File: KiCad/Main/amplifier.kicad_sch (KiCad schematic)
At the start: 37 parts, among them J3 Screw_Terminal_01x03, J4 Screw_Terminal_01x03, U3 TL074

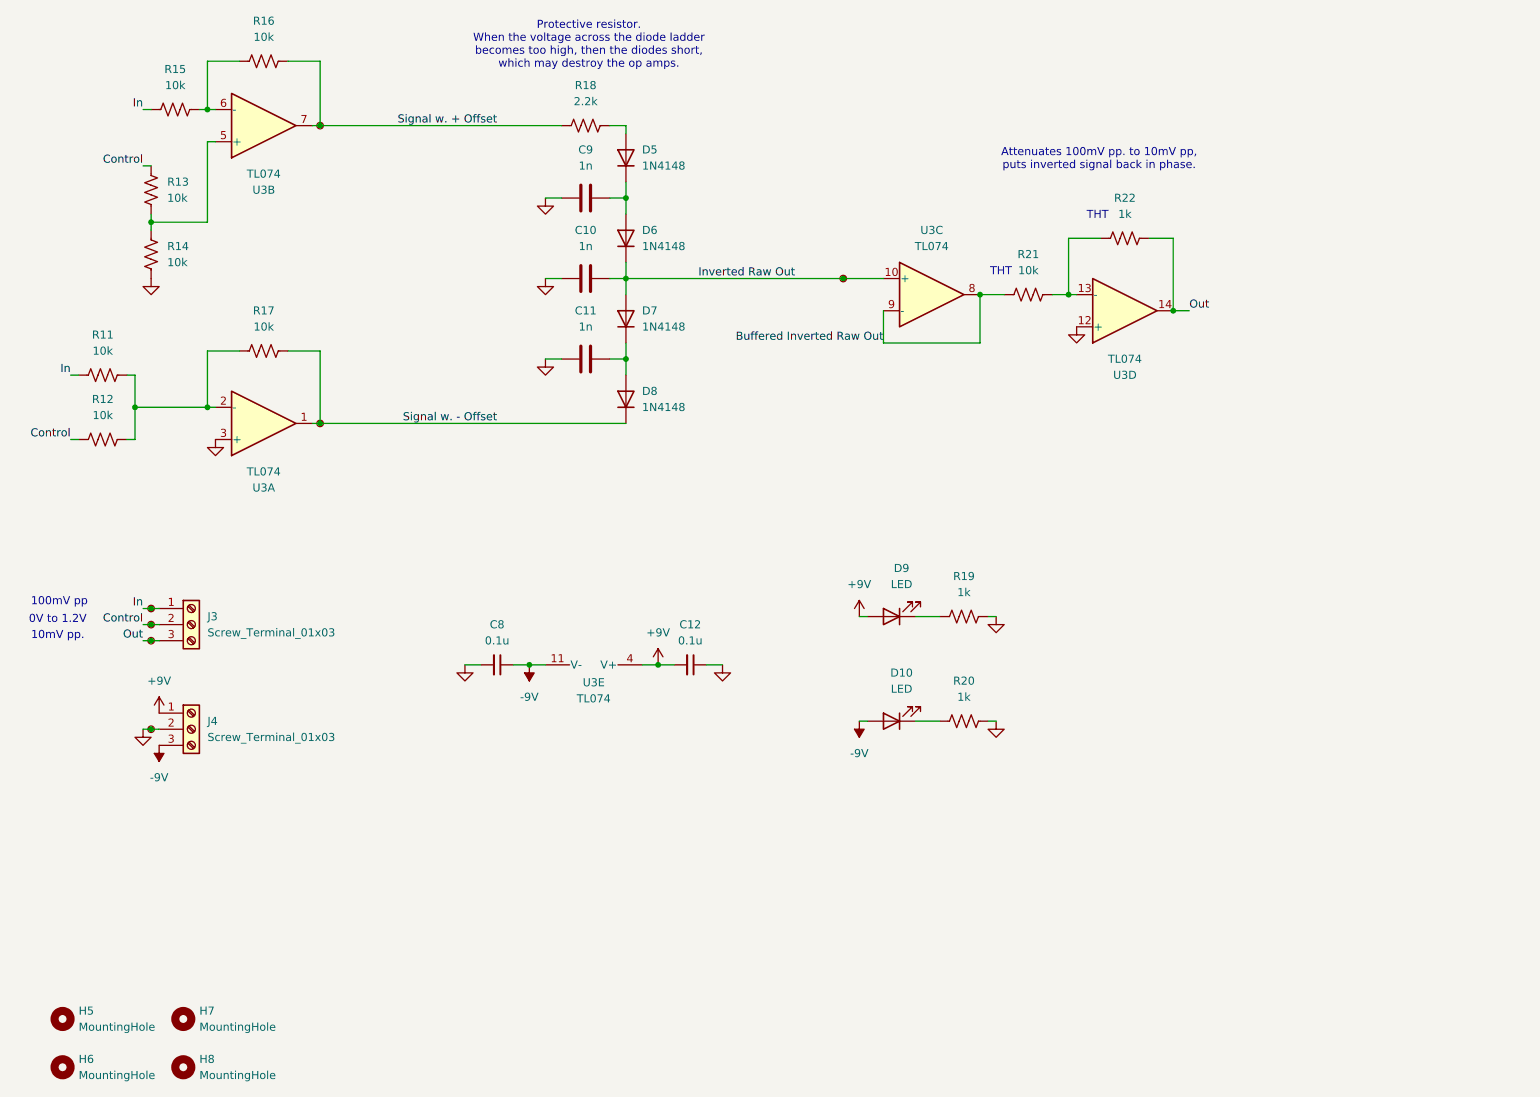
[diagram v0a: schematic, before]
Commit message: merged project into one combined board (excluding the buttons)
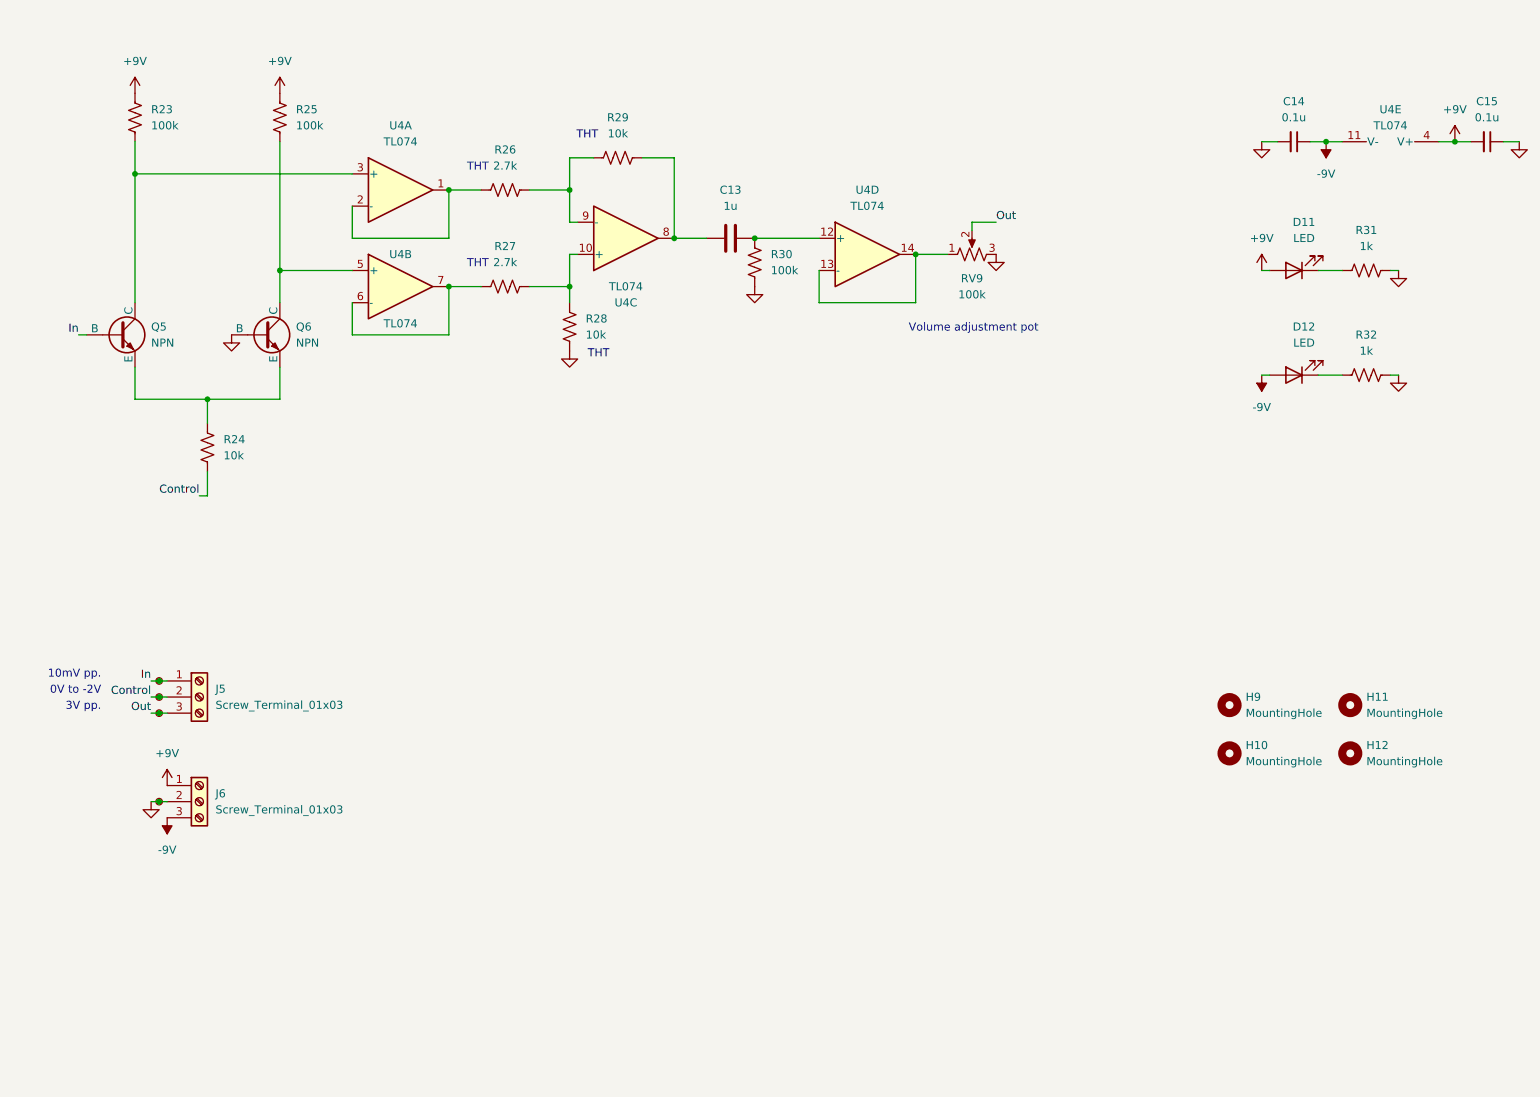
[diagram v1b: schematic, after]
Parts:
- removed C10, C11, C9: 1n, Capacitor_THT:C_Rect_L18.0mm_W5.0mm_P15.00mm_FKS3_FKP3, symbol Device:C
- removed D5, D6, D7, D8: 1N4148, Diode_THT:D_DO-35_SOD27_P7.62mm_Horizontal, symbol Diode:1N4148
- removed J3, J4: Screw_Terminal_01x03, Header 691137710003:691137710003, symbol Connector:Screw_Terminal_01x03
- removed R11, R12, R13, R14, R15, R16, R17: 10k, Resistor_SMD:R_0805_2012Metric, symbol Device:R_US
- removed R18: 2.2k, Resistor_SMD:R_0805_2012Metric, symbol Device:R_US
- removed R21: 10k, Resistor_THT:R_Axial_DIN0207_L6.3mm_D2.5mm_P7.62mm_Horizontal, symbol Device:R_US
- removed R22: 1k, Resistor_THT:R_Axial_DIN0207_L6.3mm_D2.5mm_P7.62mm_Horizontal, symbol Device:R_US
- removed TP10, TP11, TP12, TP6, TP7, TP8: TestPoint_Small, TestPoint:TestPoint_Keystone_5000-5004_Miniature, symbol Connector:TestPoint_Small
- removed U3: TL074, Package_DIP:DIP-14_W7.62mm, symbol Amplifier_Operational:TL074
- added C13: 1u, Capacitor_THT:C_Rect_L7.2mm_W4.5mm_P5.00mm, symbol Device:C
- added J5, J6: Screw_Terminal_01x03, Header 691137710003:691137710003, symbol Connector:Screw_Terminal_01x03
- added Q5, Q6: NPN, Package_TO_SOT_THT:TO-92, symbol Simulation_SPICE:NPN
- added R23, R25, R30: 100k, Resistor_SMD:R_0805_2012Metric, symbol Device:R_US
- added R24: 10k, Resistor_SMD:R_0805_2012Metric, symbol Device:R_US
- added R26, R27: 2.7k, Resistor_THT:R_Axial_DIN0207_L6.3mm_D2.5mm_P7.62mm_Horizontal, symbol Device:R_US
- added R28, R29: 10k, Resistor_THT:R_Axial_DIN0207_L6.3mm_D2.5mm_P7.62mm_Horizontal, symbol Device:R_US
- added RV9: 100k, Potentiometer_THT:Potentiometer_Bourns_PTV09A-2_Single_Horizontal, symbol Device:R_Potentiometer_US
- added TP14, TP15, TP16: TestPoint_Small, TestPoint:TestPoint_Keystone_5000-5004_Miniature, symbol Connector:TestPoint_Small
- added U4: TL074, Package_DIP:DIP-14_W7.62mm, symbol Amplifier_Operational:TL074
- renumbered C8 to C14, C12 to C15, D9 to D11, D10 to D12, H6 to H10, H7 to H11, H8 to H12, H5 to H9, R19 to R31, R20 to R32, TP9 to TP13
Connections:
- net +9V: now also J6.1 (Pin_1), R23.1, R25.1, U4.4 (V+)
- net -9V: now also J6.3 (Pin_3), U4.11 (V-)
- net Control: now also J5.2 (Pin_2), R24.2, TP14.1
- net GND: now also J6.2 (Pin_2), Q6.2 (B), R28.2, R30.2, RV9.3, TP16.1; no longer TP13.1
- net In: now also TP13.1, J5.1 (Pin_1), Q5.2 (B)
- net Out: now also J5.3 (Pin_3), RV9.2, TP15.1
- new net: C13.2, R30.1, U4.12 (+)
- new net: RV9.1, U4.13 (-), U4.14
- new net: R27.2, R28.1, U4.10 (+)
- new net: Q5.3 (E), Q6.3 (E), R24.1
- new net: R26.1, U4.1, U4.2 (-)
- new net: Q5.1 (C), R23.2, U4.3 (+)
- new net: C13.1, R29.2, U4.8
- new net: R26.2, R29.1, U4.9 (-)
- new net: Q6.1 (C), R25.2, U4.5 (+)
- new net: R27.1, U4.6 (-), U4.7
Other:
- note added: "0V to -2V"
- note added: "3V pp."
- note added: "Volume adjustment pot"
- note removed: "0V to 1.2V"
- note removed: "100mV pp"
- note removed: "Attenuates 100mV pp. to 10mV pp, puts inverted signal back in phase."
- note removed: "Protective resistor. When the voltage across the diode ladder becomes too high, then the diodes short, which may destroy the op amps."
- moved on the sheet: C14, C15, D11, D12, H10, H11, H12, H9, R31, R32
